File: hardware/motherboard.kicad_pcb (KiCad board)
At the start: 2 copper layers, 200 x 150 mm, 318 parts, among them J1 24 V DC input, J10 AX0: EN, STEP, DIR, GND, J11 AX1: EN, STEP, DIR, GND, J12 General outputs 0-7; pin9 fie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, J13 Encoder 0: +5,A,B,Z,GND, J14 Encoder 1: +5,A,B,Z,GND, J15 Encoder 2: +5,A,B,Z,GND, J16 Keyboard KIN0-7 / KOUT0-7, J17 Keyboard power/reference, J18 I2C0, J19 Full-size SD, SPI, J20 ESP-01S socket, J22 LCD LVDS 2x10, 2.00 mm, J24 AI0/GND/AI1/GND/AI2/GND, J25 0-10 V outputs 0-3; pin 1 = c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, J26 Dedicated START button input, J27 Expansion inputs 4-7; 1=GND, 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, J28 AX2: EN, STEP, DIR, GND, J29 AX3: EN, STEP, DIR, GND, J30 AX4: EN, STEP, DIR, GND, J31 Motion AUX open-drain output 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, J32 General outputs 8-15; DO_COM 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, J33 General outputs field +V and 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, J34 PLC positions 5-8 of J7 bank;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, J35 PLC positions 5-8 of J8 bank;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, J4 SWD, J5 Dedicated E-stop loop, J6 Dedicated HOLD button input, J7 PLC inputs 1-8; alternating i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, J8 PLC inputs 9-16; alternating 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, J9 Expansion inputs 0-3; 1=GND, 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, Q1 IRF7240PBF, Q5 BSS138, Q6 BSS138, Q7 BSS138, SW2 ESP_PROG, U1 LMR36510ADDAR, U10 74HC595D, U11 74HC595D, U12 74HC595D, U13 74HC595D, U18 LTV-847S, U19 LTV-847S, U2 AMS1117-3.3, U20 LTV-847S, U21 LTV-847S, U24 SN74AHCT541DW, U25 SN74AHCT541DW, U26 ULN2003ADR, U27 ULN2003ADR, U28 SN74AHCT541DW, U34 AMS1117-3.3, U35 EL3H7, U36 EL3H7, U37 L78L12ACUTR, U38 TLV2374IDR, U39 EL3H7, U40 TBA2-0512, U41 DS90LV047A, U6 74HC165D, U7 74HC165D, U8 74HC165D, U9 74HC165D

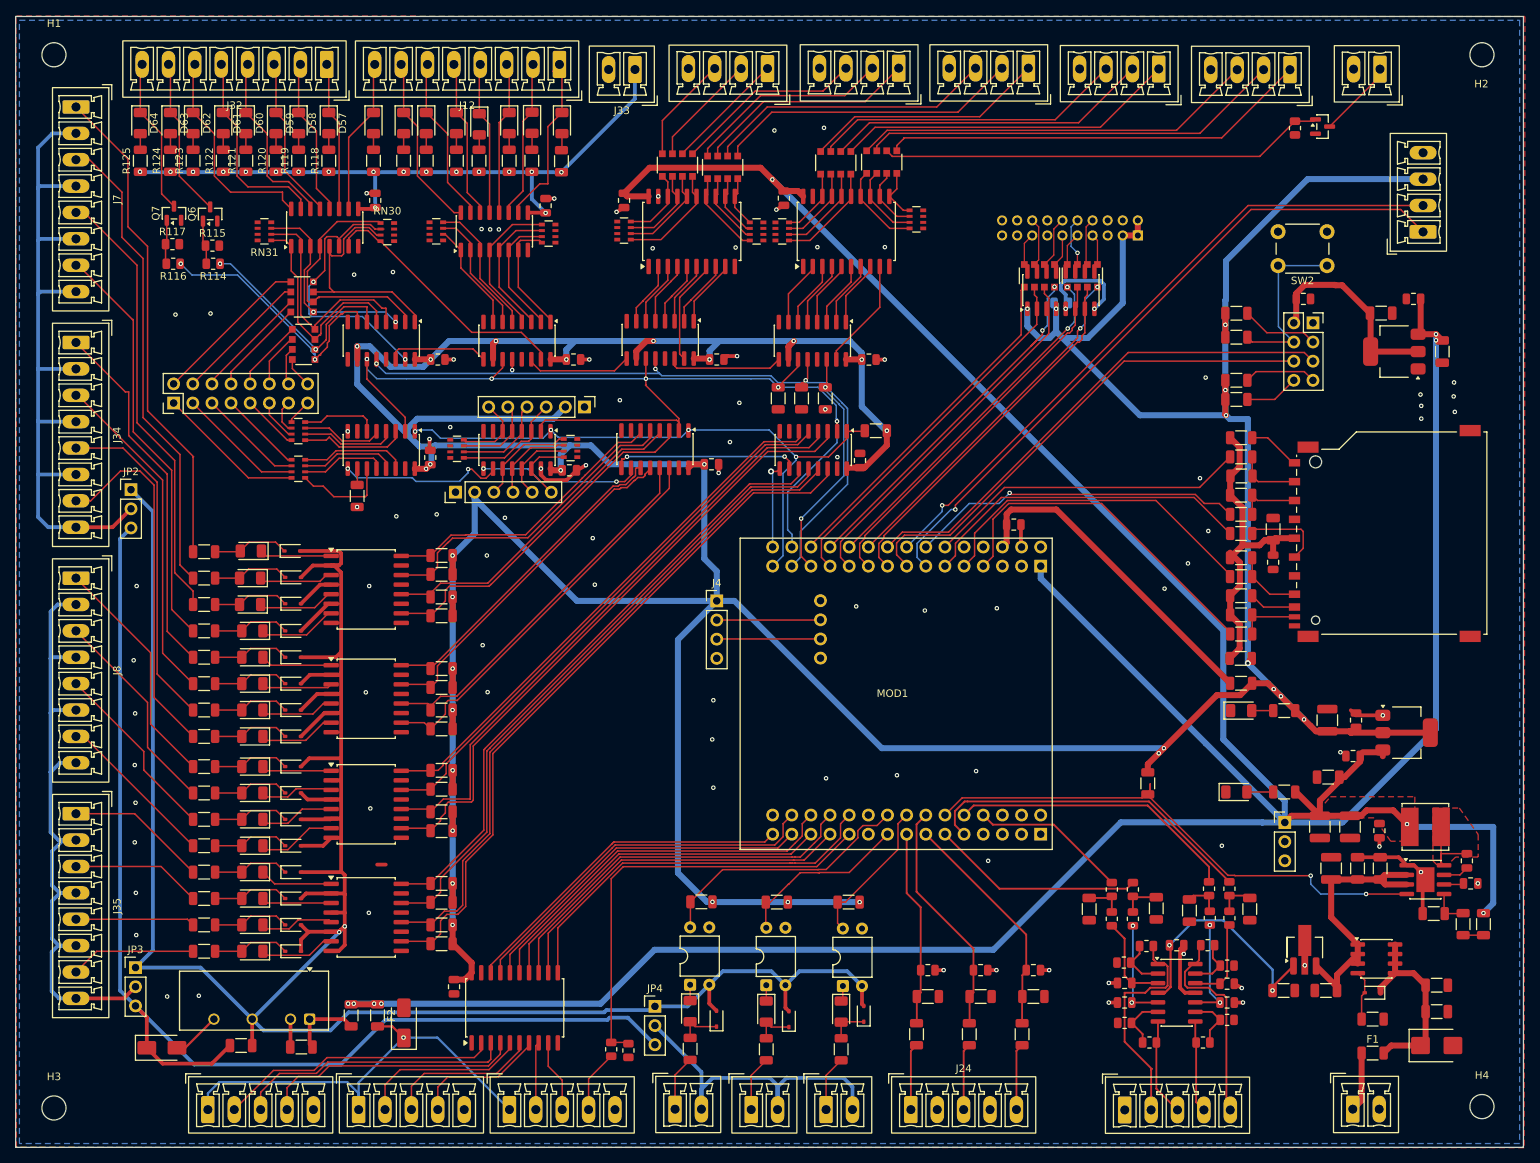
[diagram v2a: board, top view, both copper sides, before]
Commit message: Update RP2350 board power and I/O design
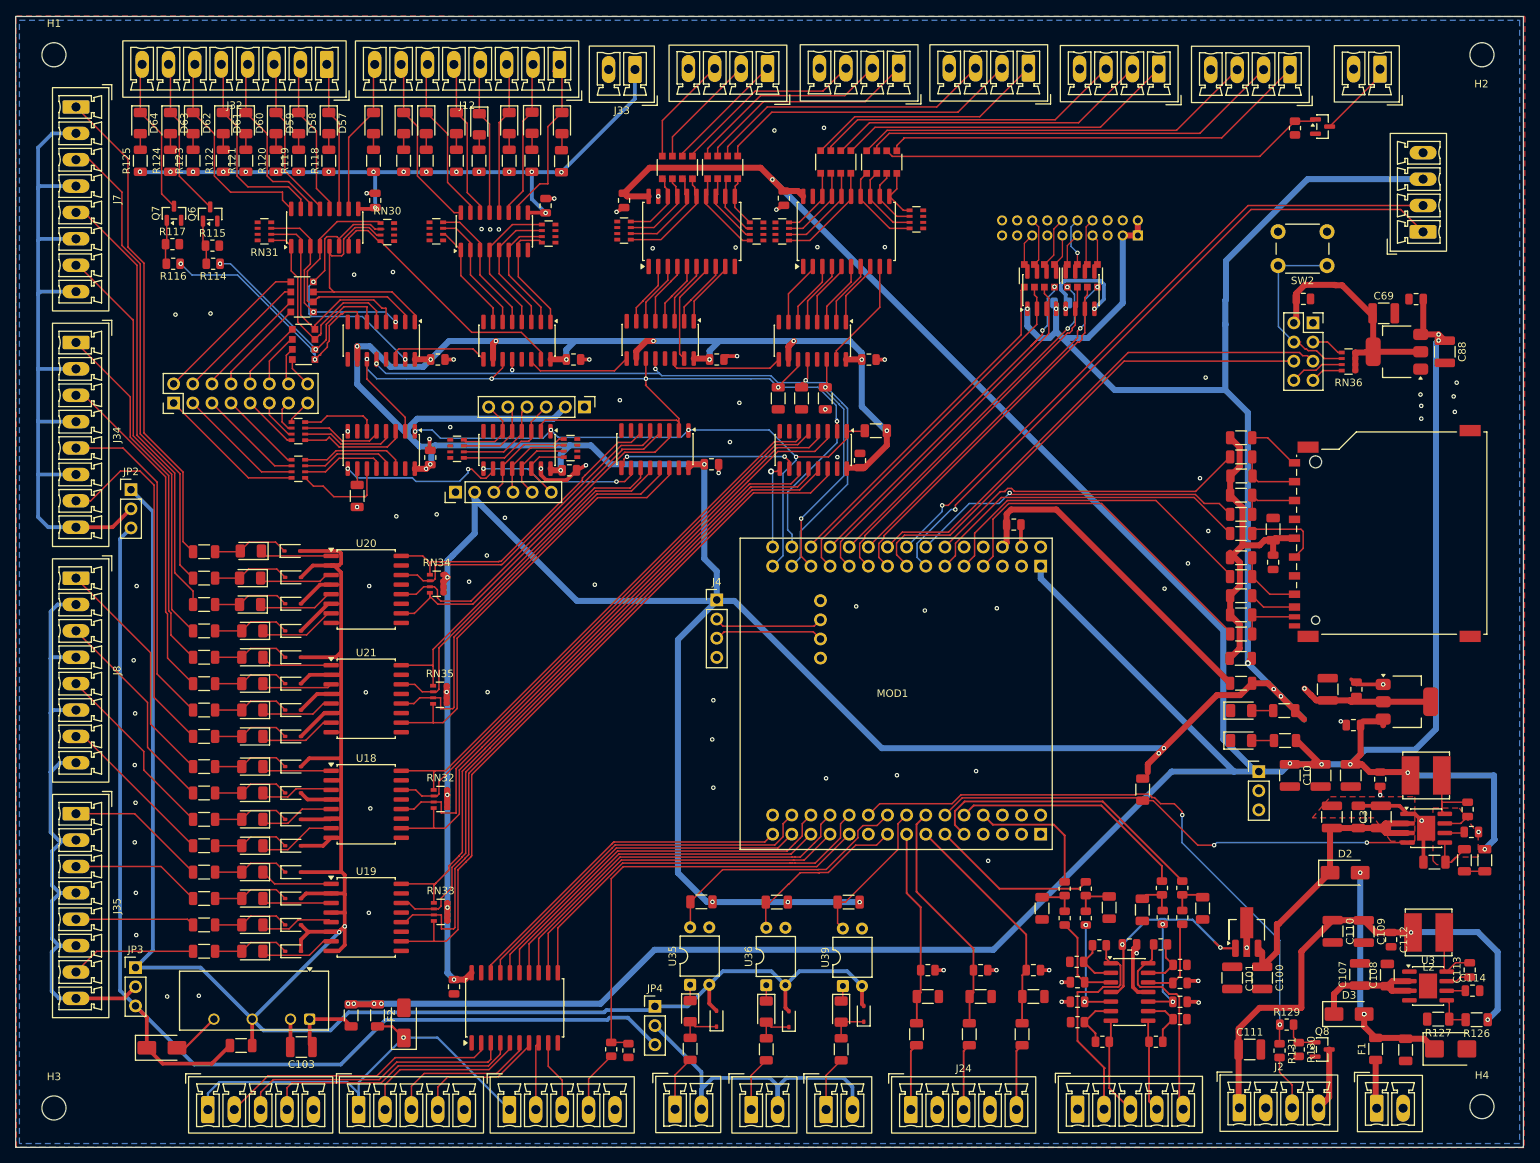
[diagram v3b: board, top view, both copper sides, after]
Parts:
- removed C1: 10uF 50V, C_1206_3216Metric
- removed Q1: IRF7240PBF, SOIC-8_3.9x4.9mm_P1.27mm
- removed R1: 100k, R_1206_3216Metric
- removed R55, R56, R57, R58: 10k, R_1206_3216Metric
- removed R76, R77, R78, R79, R80, R81, R82, R83, R84, R85, R86, R87, R88, R89, R90, R91: 4.7k, R_1206_3216Metric
- added C107: 22uF 50V, C_1210_3225Metric, F.Cu at (178.3, 127.1)
- added C108: 100nF 100V, C_1206_3216Metric, F.Cu at (181.9, 127.2)
- added C109: 22uF 25V, C_1210_3225Metric, F.Cu at (178.8, 121.4)
- added C110: 22uF 25V, C_1210_3225Metric, F.Cu at (174.7, 121.3)
- added C111: 22uF 25V, C_1210_3225Metric, F.Cu at (163.7, 137.0)
- added C112: 100nF, C_0805_2012Metric, F.Cu at (182.4, 122.5)
- added C113: 100nF, C_0805_2012Metric, F.Cu at (192.9, 126.5)
- added C114: 1uF, C_0805_2012Metric, F.Cu at (193.2, 129.2)
- added D3: SS16, D_SMA, F.Cu at (176.9, 132.3)
- added J2: Backlight: +12V, GND, PWM, switched low-side, PhoenixContact_MCV_1,5_4-G-3.5_1x04_P3.50mm_Vertical, F.Cu at (162.3, 144.8)
- added L2: 47uH 1.5A, L_Bourns_SRN6045TA, F.Cu at (187.4, 121.5)
- added Q8: BSS138, SOT-23, F.Cu at (173.3, 137.0)
- added R126: 100k, R_1206_3216Metric, F.Cu at (193.8, 133.1)
- added R127: 9.09k, R_1206_3216Metric, F.Cu at (188.7, 133.0)
- added R129: 100R, R_0805_2012Metric, F.Cu at (168.6, 133.7)
- added R130: 100k, R_0805_2012Metric, F.Cu at (170.2, 137.0)
- added R131: 100R, R_0805_2012Metric, F.Cu at (167.7, 137.2)
- added RN32: 4x4.7k, R_Array_Convex_4x0603, F.Cu at (56.4, 103.8)
- added RN33: 4x4.7k, R_Array_Convex_4x0603, F.Cu at (56.4, 118.8)
- added RN34: 4x4.7k, R_Array_Convex_4x0603, F.Cu at (55.9, 75.2)
- added RN35: 4x4.7k, R_Array_Convex_4x0603, F.Cu at (56.3, 90.0)
- added RN36: 4x10k, R_Array_Convex_4x0603, F.Cu at (176.8, 45.8)
- added U3: LMR36510ADDAR, SOIC-8-1EP_3.9x4.9mm_P1.27mm_EP2.41x3.3mm, F.Cu at (187.3, 128.6)
- C10, C103, C69, C88: value 10uF -> 22uF 25V; footprint C_1206_3216Metric -> C_1210_3225Metric
- C100: value 1uF 50V -> 22uF 50V; footprint C_1206_3216Metric -> C_1210_3225Metric
- C101: value 10uF 25V -> 22uF 25V; footprint C_1206_3216Metric -> C_1210_3225Metric
- C11, C6: value 22uF 10V -> 22uF 25V
- C3: value 10uF 50V -> 22uF 50V; footprint C_1206_3216Metric -> C_1210_3225Metric
- C90: value 22uF -> 22uF 25V
- D2: value MMSZ5242B -> SS16; footprint D_SOD-323 -> D_SMA
- moved D2 16.3 mm to (176.3, 113.6), turned to 0 degrees
- moved C100 8.61 mm to (165.3, 127.5), turned to -90 degrees
- moved R70 8.48 mm to (194.9, 111.9)
- moved R71 8.48 mm to (192.2, 111.9)
- moved U37 8.05 mm to (163.3, 121.2)
- moved J17 7.58 mm to (164.9, 100.2)
- moved C101 7.03 mm to (161.4, 127.5), turned to -90 degrees
- moved D4 6.85 mm to (162.6, 96.0)
- moved C11 6.83 mm to (173.1, 100.7)
- moved C3 6.83 mm to (181.1, 106.2)
- moved C4 6.83 mm to (178.1, 106.2)
- moved C5 6.83 mm to (174.6, 106.2)
- moved C6 6.83 mm to (177.1, 100.7)
- moved C7 6.83 mm to (181.0, 101.2)
- moved C86 6.83 mm to (192.6, 105.2)
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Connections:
- D2 pad 1: VIN_FUSED -> VIN_PROT
- D2 pad 2: Q1_GATE -> VIN_FUSED
- MOD1 pad 25: (no net) -> BL_PWM_MCU
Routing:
- net BL_PWM_MCU: track 0.00 -> 80.0 mm, vias 0 -> 2
- net +12V_BL: track 0.00 -> 66.8 mm, vias 0 -> 2
- net +5V: track 475.3 -> 446.2 mm, vias 9 -> 12
- net +3V3: track 696.6 -> 678.7 mm, vias 35 -> 29
- net VIN_BL_PROT: track 0.00 -> 16.6 mm
- net BUCK12_SW: track 0.00 -> 8.86 mm
- net BL_LED_N: track 0.00 -> 8.33 mm
- net BL_PWM: track 0.00 -> 7.38 mm
- net Q1_GATE: track 6.65 -> 0.00 mm
- net AOUT2_PWM: track 38.4 -> 32.1 mm
- net AOUT3_PWM: track 44.9 -> 38.6 mm
- net AOUT1_PWM: track 28.3 -> 22.1 mm
- net +12V_AO: track 32.5 -> 26.6 mm
- net PWR_GOOD_N: track 71.2 -> 65.3 mm
- net WIFI_GPIO2: track 10.3 -> 4.42 mm
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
